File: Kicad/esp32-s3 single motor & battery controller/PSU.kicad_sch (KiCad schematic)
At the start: 70 parts, among them J5 Batt Balance connector, Q1 NMOS,12v, Q2 NMOS, 12v, Q3 NMOS,12v,PPak, Q4 NMOS, 12v, Q5 NMOS, 12v, Q7 NMOS,12v,PPak, U2 AP63203WU, U3 BQ76905RGRR, U4 BQ24780SRUYR

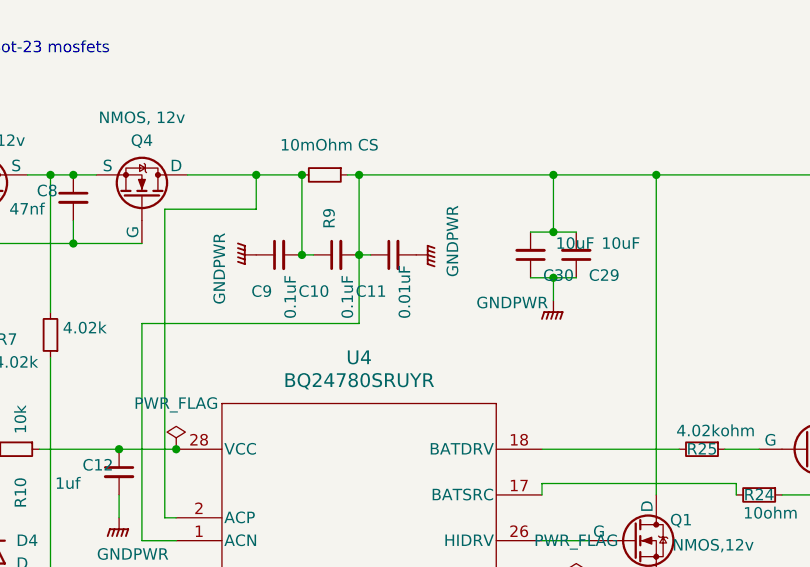
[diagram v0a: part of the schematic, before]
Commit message: Almost complete charger section, working on balancer
I have a problem with the current sense lines on the balance charger. One loops around with filter capacitors, while the other zigs and zags back and forth on multiple layers! They have to cross each other, and this may lead to a lot of noise.
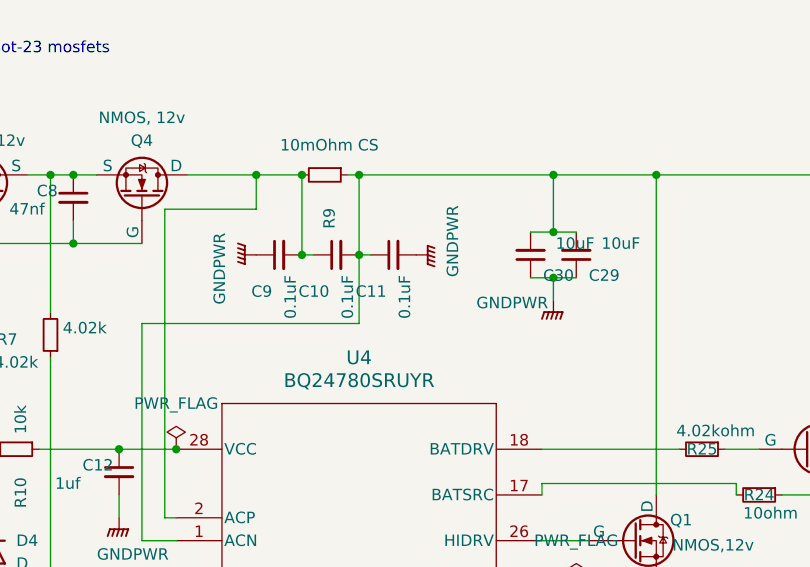
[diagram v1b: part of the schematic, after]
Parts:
- C11: value 0.01uF -> 0.1uF
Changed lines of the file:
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@@
 			)
 		)
-		(property "Value" "0.01uF"
+		(property "Value" "0.1uF"
 			(at 78.74 80.772 0)
 			(effects

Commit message: Finished PCB with 2s battery charger
Silkscreen is all finished
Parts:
- added C41: 220uF, Capacitor_SMD:CP_Elec_6.3x9.9, symbol Device:C
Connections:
- net GNDPWR: now also C41.2
- net MOTORPWR: now also C41.1
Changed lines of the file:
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@@
 	)
 	(junction
+		(at 119.38 64.77)
+		(diameter 0)
+		(color 0 0 0 0)
+	)
+	(junction
 		(at 173.99 158.75)
 		(diameter 0)
@@
 	(wire
 		(pts
-			(xy 125.73 64.77) (xy 106.68 64.77)
+			(xy 125.73 64.77) (xy 119.38 64.77)
 		)
 		(stroke
@@
 	(wire
 		(pts
+			(xy 119.38 64.77) (xy 106.68 64.77)
+		)
+		(stroke
+			(width 0)
+			(type default)
+		)
+	)
+	(wire
+		(pts
 			(xy 144.78 118.11) (xy 157.48 118.11)
 		)
@@
 	)
 	(symbol
+		(lib_id "Device:C")
+		(at 119.38 68.58 0)
+		(unit 1)
+		(exclude_from_sim no)
+		(in_bom yes)
+		(on_board yes)
+		(dnp no)
+		(property "Reference" "C41"
+			(at 121.412 67.564 0)
+			(effects
+				(font
+					(size 1.27 1.27)
+				)
+				(justify left)
+			)
+		)
+		(property "Value" "220uF"
+			(at 122.174 70.358 0)
+			(effects
+				(font
+					(size 1.27 1.27)
+				)
+				(justify left)
+			)
+		)
+		(property "Footprint" "Capacitor_SMD:CP_Elec_6.3x9.9"
+			(at 120.3452 72.39 0)
+			(effects
+				(font
+					(size 1.27 1.27)
+				)
+				(hide yes)
+			)
+		)
+		(property "Datasheet" "~"
+			(at 119.38 68.58 0)
+			(effects
+				(font
+					(size 1.27 1.27)
+				)
+				(hide yes)
+			)
+		)
+		(property "Description" "Unpolarized capacitor"
+			(at 119.38 68.58 0)
+			(effects
+				(font
+					(size 1.27 1.27)
+				)
+				(hide yes)
+			)
+		)
+		(pin "1"
+		)
+		(pin "2"
+		)
+		(instances
+			(project ""
+				(path "/eb3f183d-8bb1-43a5-a363-092ed67891e3/a57a0b4f-e246-497c-8d94-688647d8fd03"
+					(reference "C41")
+					(unit 1)
+				)
+			)
+		)
+	)
+	(symbol
 		(lib_id "power:GNDPWR")
 		(at 245.11 73.66 0)
@@
 					(unit 1)
 				)
+			)
+		)
+	)
+	(symbol
+		(lib_id "power:GNDPWR")
+		(at 119.38 72.39 0)
+		(unit 1)
+		(exclude_from_sim no)
+		(in_bom yes)
+		(on_board yes)
+		(dnp no)
+		(property "Reference" "#PWR050"
+			(at 119.38 77.47 0)
+			(effects
+				(font
+					(size 1.27 1.27)
+				)
+				(hide yes)
+			)
+		)
+		(property "Value" "GNDPWR"
+			(at 114.808 72.644 0)
+			(effects
+				(font
+					(size 1.27 1.27)
+				)
+			)
+		)
+		(property "Footprint" ""
+			(at 119.38 73.66 0)
+			(effects
+				(font
+					(size 1.27 1.27)
+				)
+				(hide yes)
+			)
+		)
+		(property "Datasheet" ""
+			(at 119.38 73.66 0)
+			(effects
+				(font
+					(size 1.27 1.27)
+				)
+				(hide yes)
+			)
+		)
+		(property "Description" "Power symbol creates a global label with name \"GNDPWR\" , global ground"
+			(at 119.38 72.39 0)
+			(effects
+				(font
+					(size 1.27 1.27)
+				)
+				(hide yes)
+			)
+		)
+		(pin "1"
+		)
+		(instances
+			(project "esp32-s3 single motor & battery controller"
+				(path "/eb3f183d-8bb1-43a5-a363-092ed67891e3/a57a0b4f-e246-497c-8d94-688647d8fd03"
+					(reference "#PWR050")
+					(unit 1)
+				)

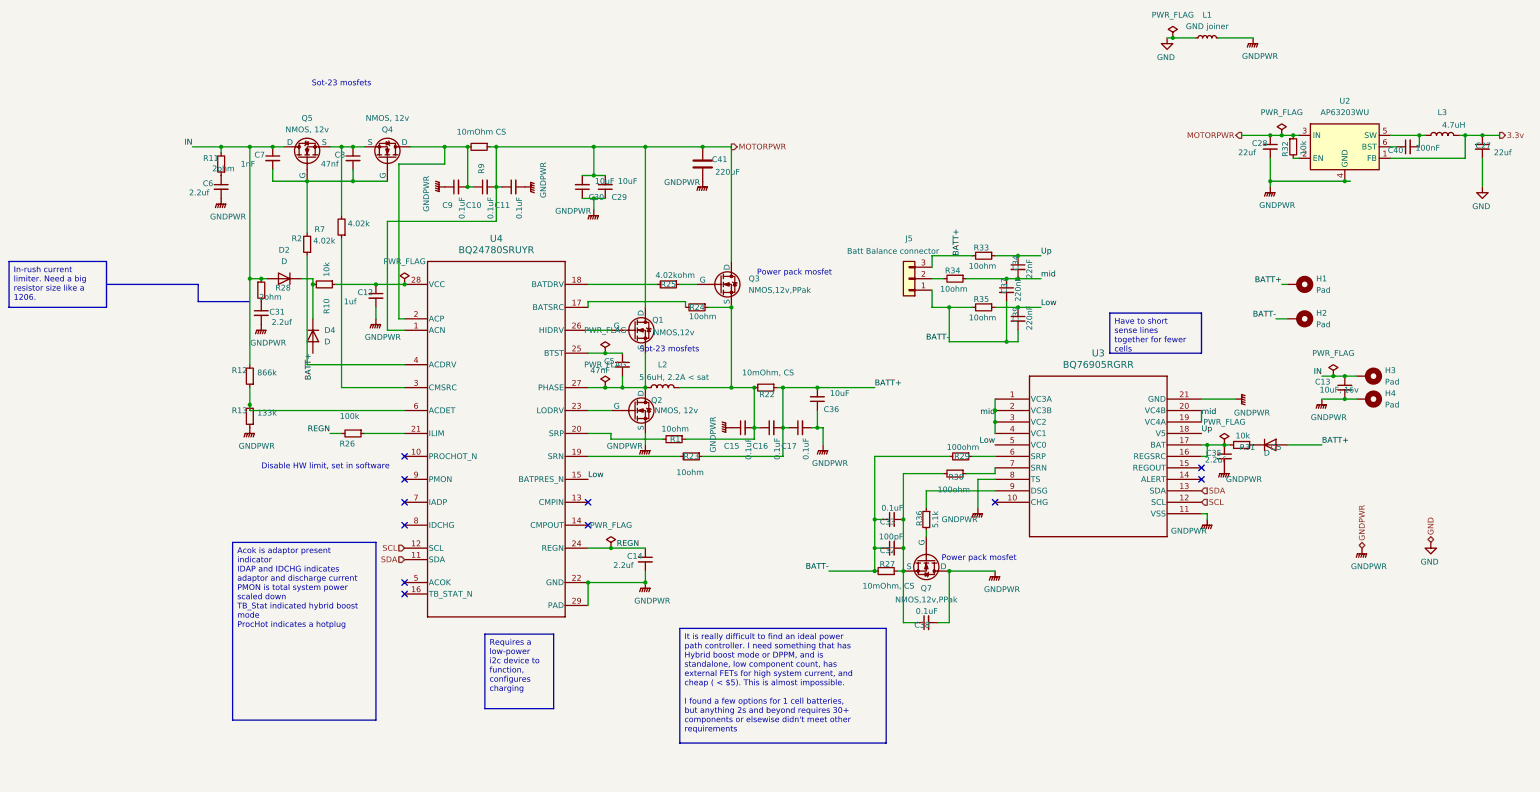
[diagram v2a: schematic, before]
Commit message: Removed battery voltage divider, fixed BATTPres indicator
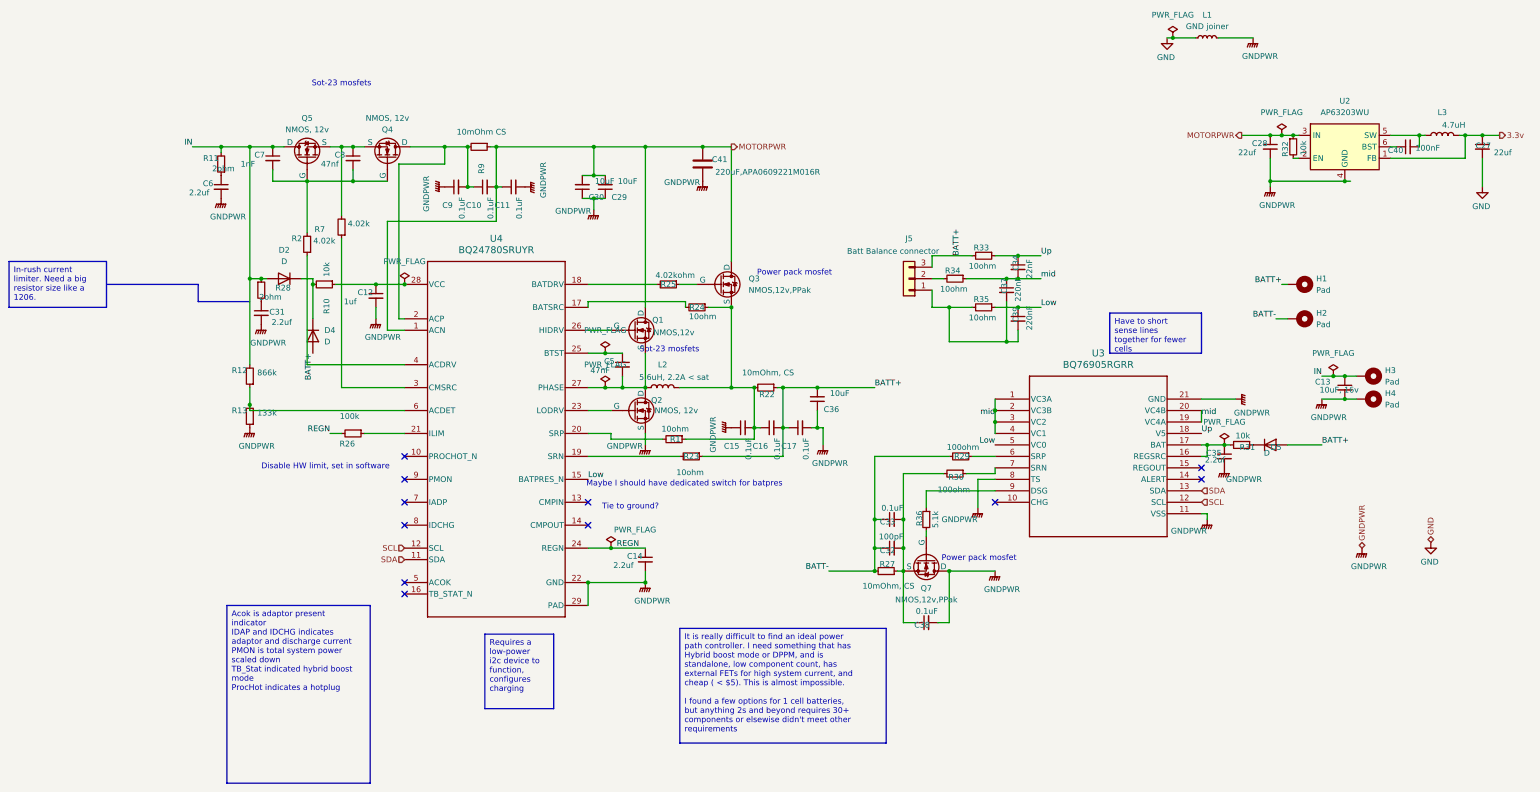
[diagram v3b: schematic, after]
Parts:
- C41: value 220uF -> 220uF,APA0609221M016R
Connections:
- net BATT-: no longer C37.2, C39.2, J5.1 (Pin_1), R35.2
- new net: C37.2, C39.2, J5.1 (Pin_1), R35.2
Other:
- note added: "Maybe I should have dedicated switch for batpres"
- note added: "Tie to ground?"
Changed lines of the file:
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@@
 	(text_box "Acok is adaptor present indicator\nIDAP and IDCHG indicates adaptor and discharge current\nPMON is total system power scaled down\nTB_Stat indicated hybrid boost mode\nProcHot indicates a hotplug"
 		(exclude_from_sim no)
-		(at 15.24 152.4 0)
+		(at 13.97 166.37 0)
 		(size 31.75 39.37)
 		(stroke
@@
 		)
 	)
+	(text "Maybe I should have dedicated switch for batpres"
+		(exclude_from_sim no)
+		(at 115.316 139.446 0)
+		(effects
+			(font
+				(size 1.27 1.27)
+			)
+		)
+	)
+	(text "Tie to ground?"
+		(exclude_from_sim no)
+		(at 103.378 144.526 0)
+		(effects
+			(font
+				(size 1.27 1.27)
+			)
+		)
+	)
 	(text "Disable HW limit, set in software"
 		(exclude_from_sim no)
@@
 	(label "REGN"
 		(at 36.83 128.27 180)
-		(fields_autoplaced yes)
-		(effects
-			(font
-				(size 1.27 1.27)
-			)
-			(justify right bottom)
-		)
-	)
-	(label "BATT-"
-		(at 173.99 107.95 180)
 		(fields_autoplaced yes)
 		(effects
@@
 			)
 		)
-		(property "Value" "220uF"
+		(property "Value" "220uF,APA0609221M016R"
 			(at 122.174 70.358 0)
 			(effects
@@
 		(on_board yes)
 		(dnp no)
-		(fields_autoplaced yes)
 		(property "Reference" "#FLG04"
 			(at 99.06 151.765 0)
@@
 		)
 		(property "Value" "PWR_FLAG"
-			(at 99.06 148.59 0)
-			(effects
-				(font
+			(at 104.394 149.606 0)
+			(effects
+				(font

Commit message: Adding usage notes and required pullup resistors
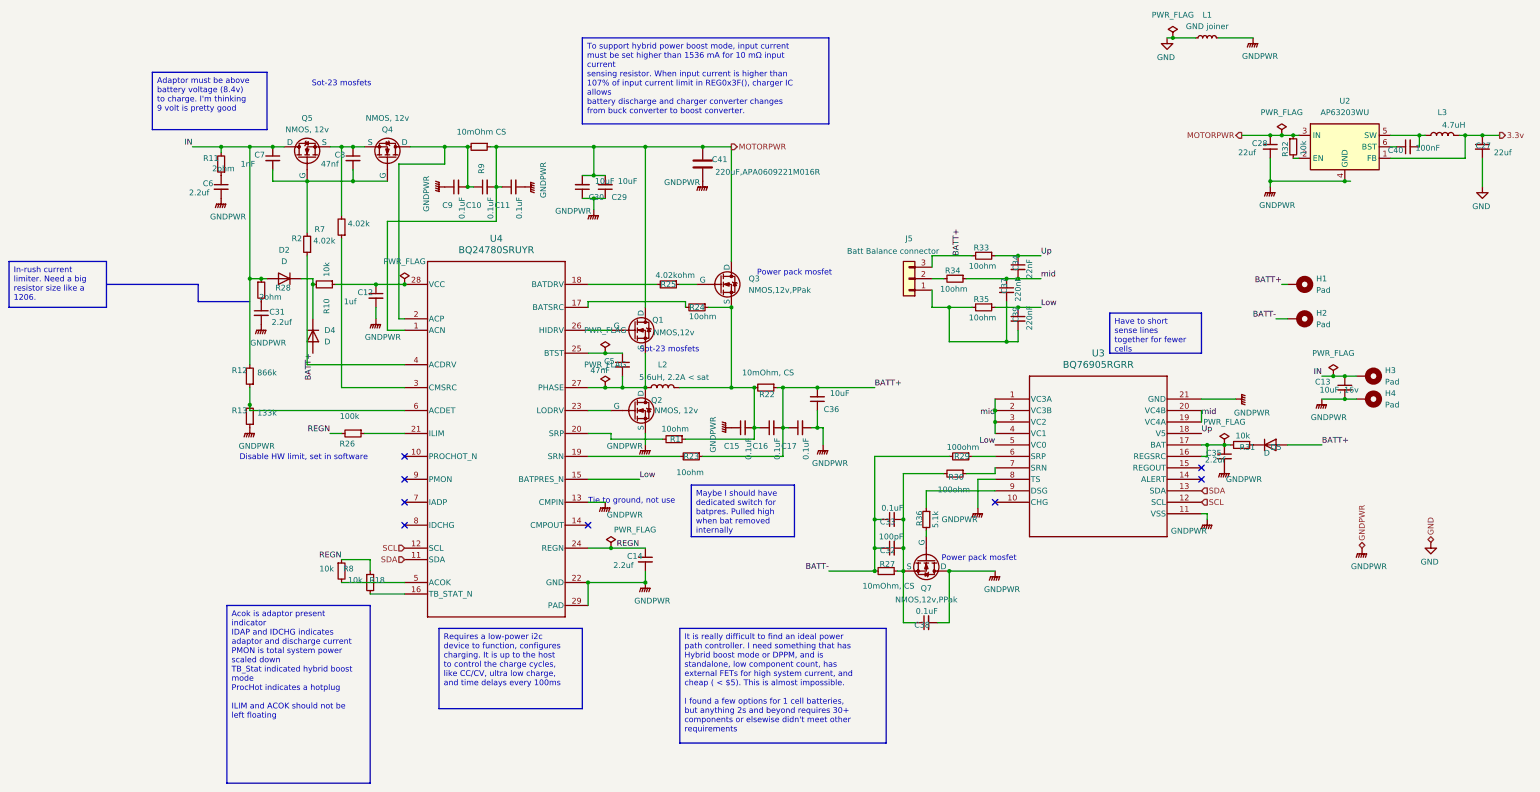
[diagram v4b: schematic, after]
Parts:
- added R18, R8: 10k, Resistor_SMD:R_0603_1608Metric, symbol Device:R_Small
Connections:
- net GNDPWR: now also U4.13 (CMPIN)
- net REGN: now also R18.1, R8.1
- net at U4.16 (TB_STAT_N): now also R18.2
- net at U4.5 (ACOK): now also R8.2
- no-connect marks 11 -> 8
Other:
- note added: "Tie to ground, not use"
- note removed: "Maybe I should have dedicated switch for batpres"
- note removed: "Tie to ground?"
